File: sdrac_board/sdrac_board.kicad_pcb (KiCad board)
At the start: 4 copper layers, 81 x 51 mm, 147 parts, among them IC1 LMR16030PDDA, J1 SWD, J10 Mag_enc, J11 Pos_zero_sens, J12 Conn_01x02, J2 SYNCHRONIZER, J3 INOUT, J4 Conn_01x02_Male, J5 Conn_01x02_Female, J6 STEPER_DRIVER_CONTROL, J7 STEPER_DRIVER_MOTOR_OUT, J8 USB_C_Receptacle_USB2.0, J9 Conn_01x02, SW1 BOOT0, SW2 NRST, SW3 USR_BTN, SW4 SW_DIP_x01, U1 STM32F412RGT6, U10 USBLC6-2SC6, U11 MCP9700AT-ETT, U2 FM24CL16B, U3 SN65HVD232, U4 CAN, U5 CAN, U6 AZ1117-3.3, U7 SN74LV1T34DBV, U8 SN74LV1T34DBV, U9 SN74LV1T34DBV, Y1 16MHz

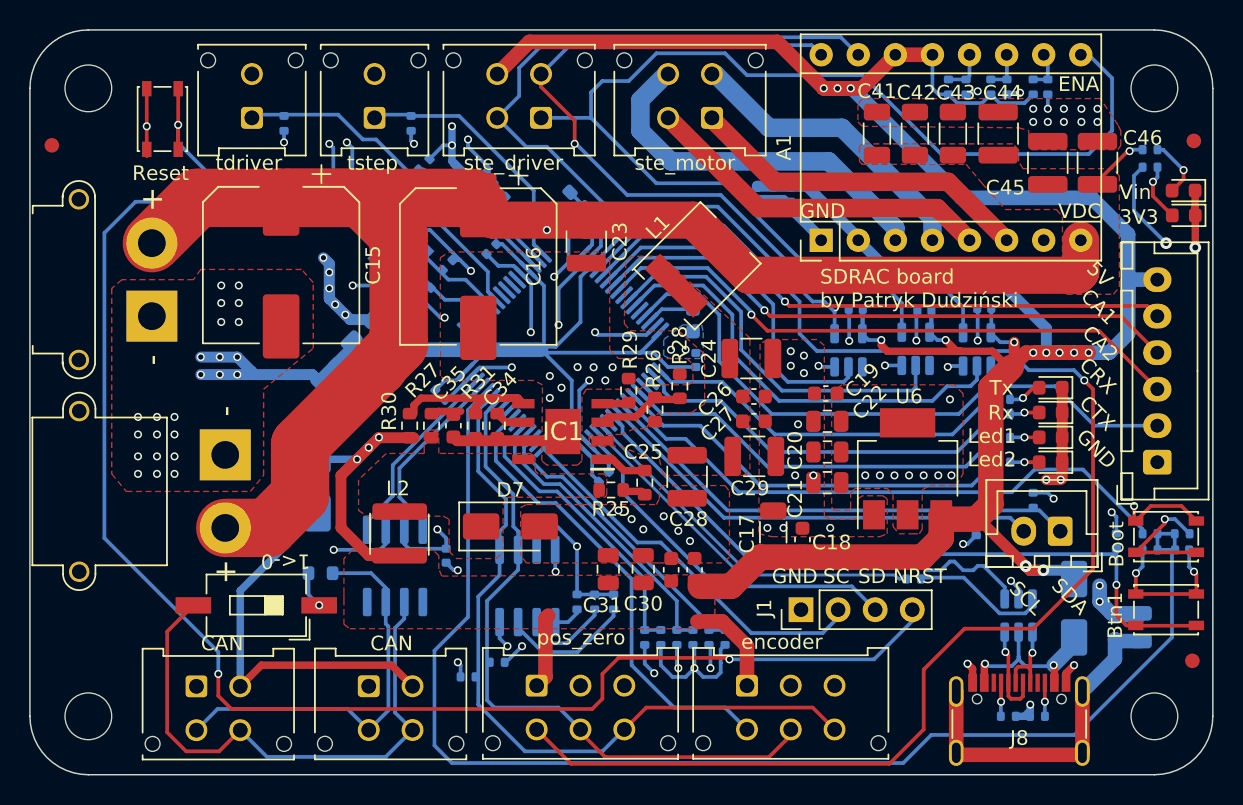
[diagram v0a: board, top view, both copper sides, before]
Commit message: added 10A screw terminal
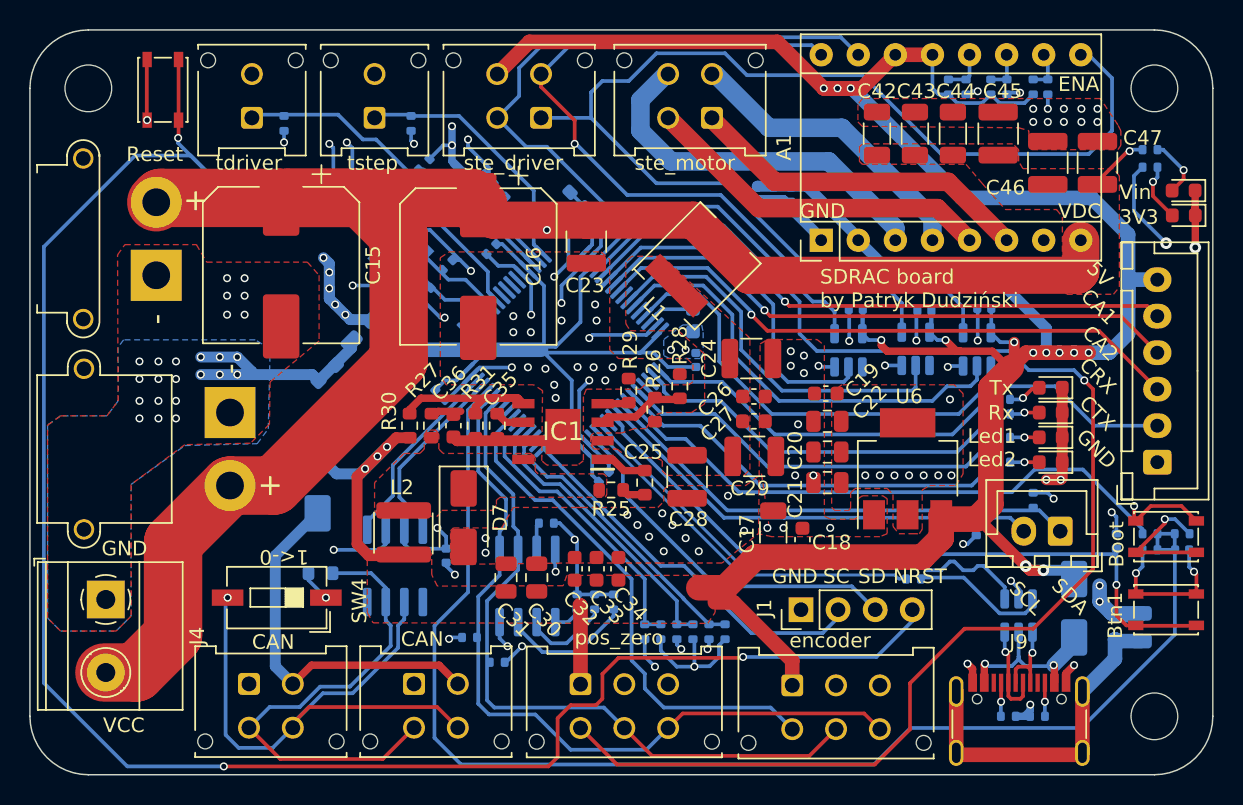
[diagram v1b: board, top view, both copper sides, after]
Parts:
- removed FID1, FID2, FID3: Fiducial, Fiducial:Fiducial_1mm_Mask2mm
- removed H4: MountingHole, MountingHole:MountingHole_3.2mm_M3_ISO7380
- added C34: 1n, Capacitor_SMD:C_0603_1608Metric, F.Cu at (141.2, 99.5)
- added J4: STEPER DRIVER VCC, TerminalBlock_Phoenix:TerminalBlock_Phoenix_MKDS-1,5-2_1x02_P5.00mm_Horizontal, F.Cu at (106.1, 101.6)
- R32: value 100k -> 43k
- R35: value 10k -> 1k
- SW4: footprint Button_Switch_SMD:SW_DIP_SPSTx01_Slide_6.7x4.1mm_W8.61mm_P2.54mm_LowProfile -> Button_Switch_SMD:SW_DIP_SPSTx01_Slide_6.7x4.1mm_W6.73mm_P2.54mm_LowProfile_JPin
- moved C30 7.32 mm to (135.6, 100.1)
- moved C31 7.02 mm to (133.5, 100.1)
- moved C33 6.71 mm to (139.7, 99.5)
- moved C32 6.61 mm to (138.2, 99.5)
- moved U4 3.60 mm to (115.9, 107.4)
- moved D7 3.26 mm to (130.6, 96.0), turned to -90 degrees
- moved U5 3.10 mm to (127.2, 107.4)
- moved J11 3.10 mm to (153.1, 107.5)
- moved J12 3.00 mm to (138.6, 107.4)
- moved J5 2.92 mm to (114.6, 88.8)
- moved J6 2.82 mm to (109.5, 79.4)
- moved R5 2.70 mm to (131.0, 104.2)
- moved SW2 2.00 mm to (110.0, 66.7)
- moved SW4 1.50 mm to (117.8, 101.5)
- moved R13 0.39 mm to (144.1, 103.8)
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- renumbered C34 to C35, C35 to C36, C36 to C37, C37 to C38, C38 to C39, C39 to C40, C40 to C41, C41 to C42, C42 to C43, C43 to C44, C44 to C45, C45 to C46, C46 to C47, C47 to C48, C48 to C49, C49 to C50, J9 to J10, J10 to J11, J11 to J12, J12 to J13, J4 to J5, J5 to J6, J6 to J7, J7 to J8, J8 to J9
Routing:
- net /MCU/NRST: track 129.8 -> 149.7 mm
- net VCC: track 111.5 -> 124.7 mm
- net /CAN/CANH: track 27.4 -> 33.3 mm
- net GND: track 164.3 -> 160.4 mm, vias 98 -> 111
- net /MCU/Mag_enc_analog: track 31.8 -> 35.4 mm
- net /MCU/Poz_zero_sens: track 100.4 -> 96.9 mm
- net /MCU/SCL: track 46.3 -> 49.1 mm
- net /MCU/SDA: track 50.6 -> 53.2 mm
- net /CAN/CANL: track 38.4 -> 40.6 mm, vias 0 -> 1
- net +3V3: track 53.7 -> 52.4 mm
- net /CAN/CAN_5V: track 27.0 -> 25.7 mm
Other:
- board text added: "CID0_0"
- board text added: "CID0_1"
- board text added: "CID1_0"
- board text added: "CID1_1"
- board text added: "CID2_0"
- board text added: "CID2_1"
- board text added: "MS1_0"
- board text added: "MS1_1"
- board text added: "MS2_0"
- board text added: "MS2_1"
- board text added: "MS3_0"
- board text added: "MS3_1"
- board text added: "VCC"
